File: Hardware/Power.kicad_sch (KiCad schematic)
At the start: 24 parts, among them IC1 TLV70130DBVR, IC2 TLV70130DBVR

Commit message: organization, updated submodule
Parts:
- D9: value 3V3 High -> 3V3 HV
- TP6: renamed from TP5; value 3V3 High -> 3V3 HV
- TP9: renamed from TP8; value GND High -> GND HV
- renumbered IC1 to IC2, IC2 to IC3, TP9 to TP10, TP4 to TP5, TP6 to TP7, TP7 to TP8
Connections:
- net +3V3 High renamed +3.3V HV
- net +3.3V HV: no longer TP6.1
- net +5V High renamed +5V HV
- net GND High renamed GND HV
- new net +3V3 HV: TP6.1
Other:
- note added: "3.3V: HV side"
- note added: "3.3V: LV side"
- note added: "HV 3V3"
- note added: "Indicators"
- note added: "Isolated"
- note added: "LV 3V3"
- note added: "MCU, CAN"
- note removed: "3.3V:"
- note removed: "Isolated 3v3"
- note removed: "Non-Isolated 3v3"
- note removed: "Status LEDs"

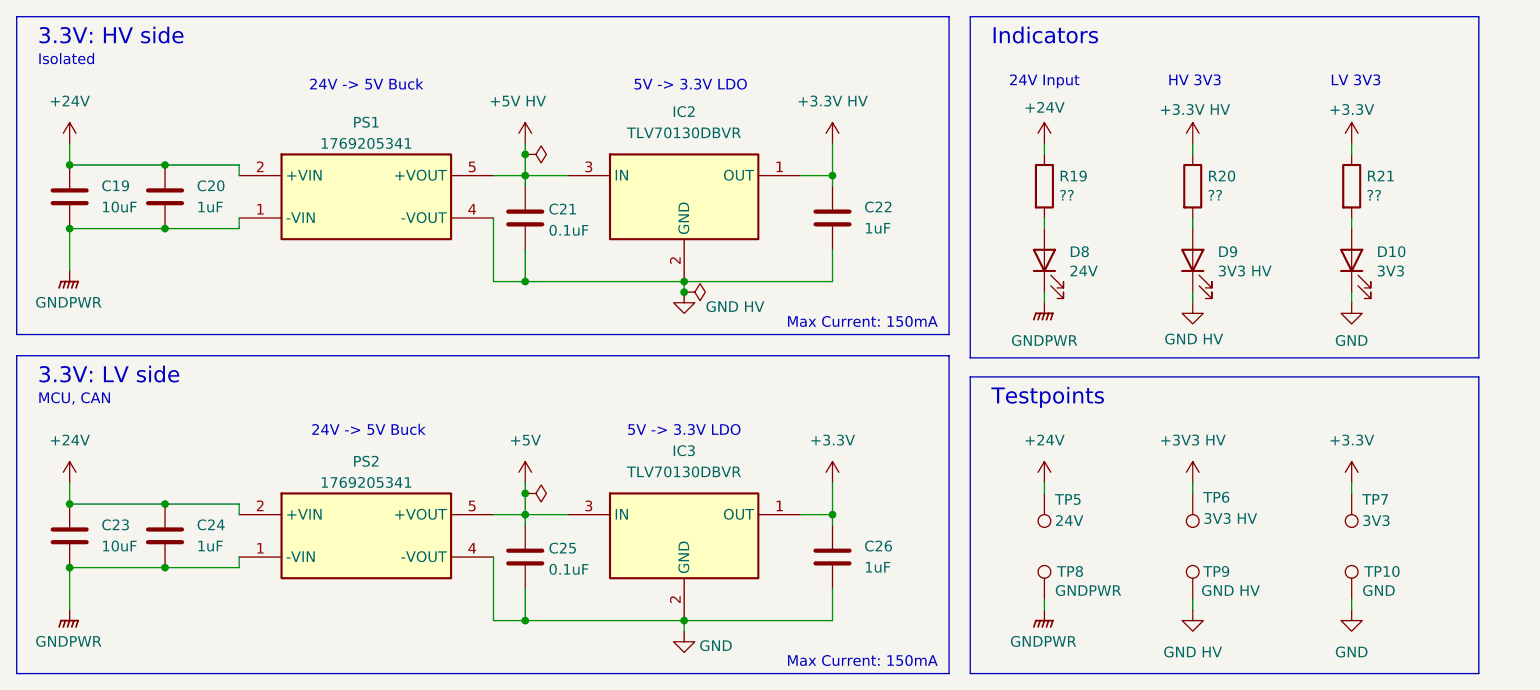
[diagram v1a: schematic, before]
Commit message: new isolated amp, filter stage; need to select values
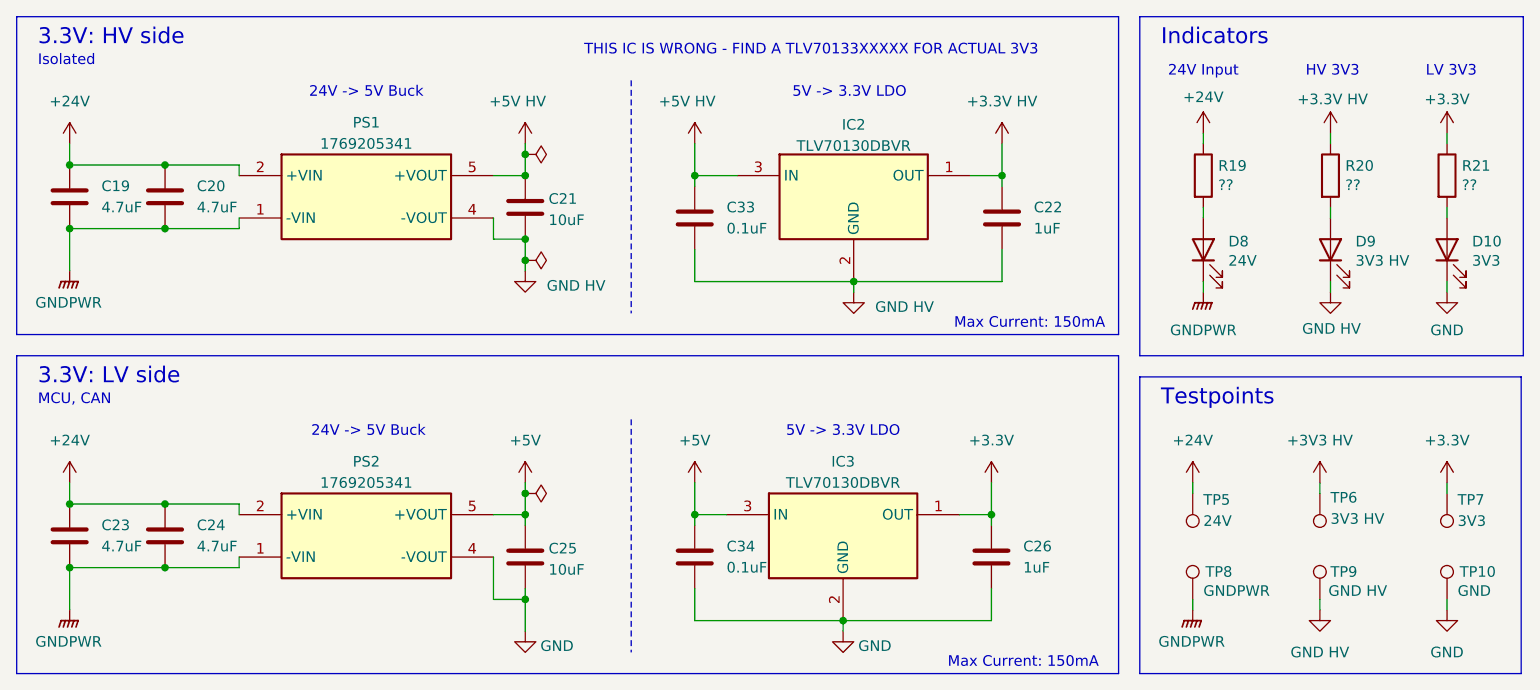
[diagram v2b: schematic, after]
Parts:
- added C33, C34: 0.1uF, Capacitor_SMD:C_0805_2012Metric, symbol Device:C
- C19, C23: value 10uF -> 4.7uF
- C20, C24: value 1uF -> 4.7uF
- C21, C25: value 0.1uF -> 10uF
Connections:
- net +5V: now also C34.1
- net +5V HV: now also C33.1
- net GND: now also C34.2
- net GND HV: now also C33.2
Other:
- note added: "THIS IC IS WRONG - FIND A TLV70133XXXXX FOR ACTUAL 3V3"
- moved on the sheet: C21, C22, C26, D10, D8, D9, IC2, IC3, R19, R20, R21, TP10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

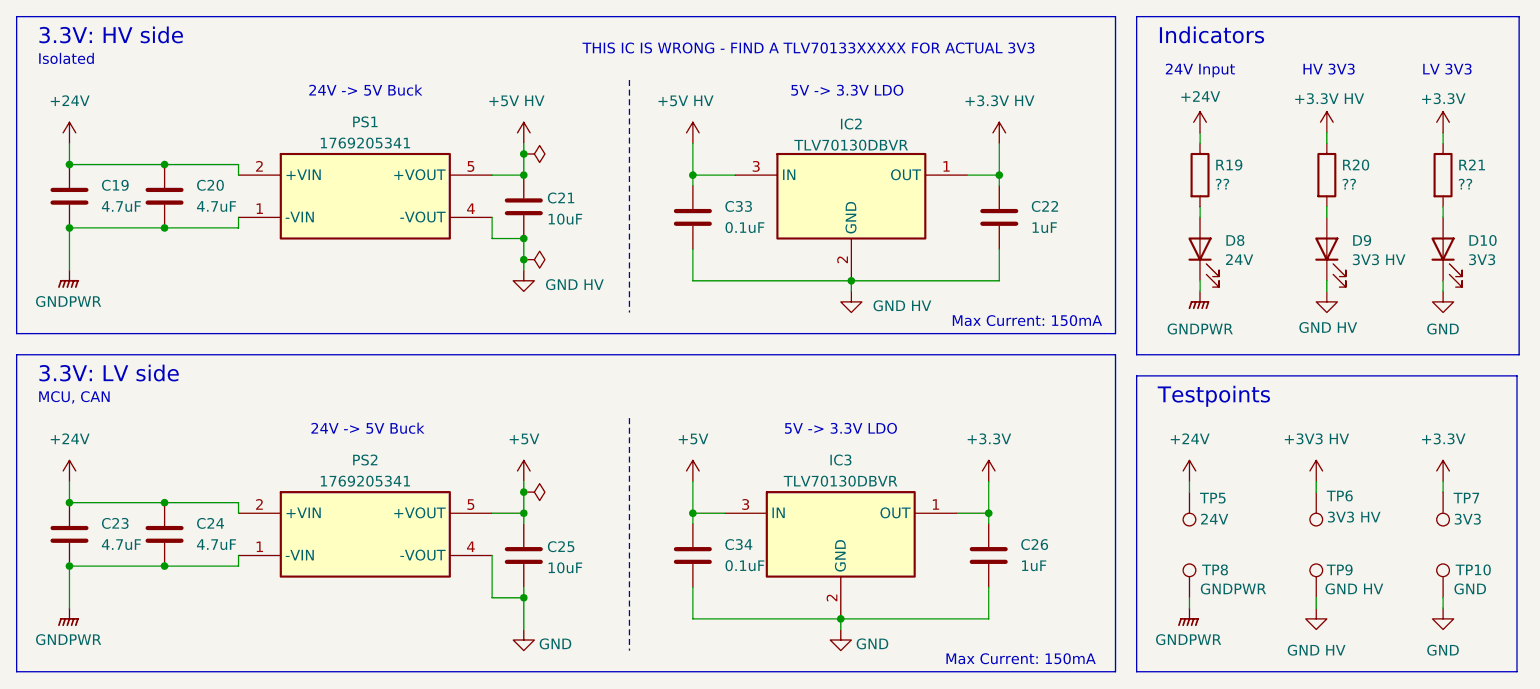
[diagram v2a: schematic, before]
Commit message: added LEDs, changed LDO, still need to address other comments
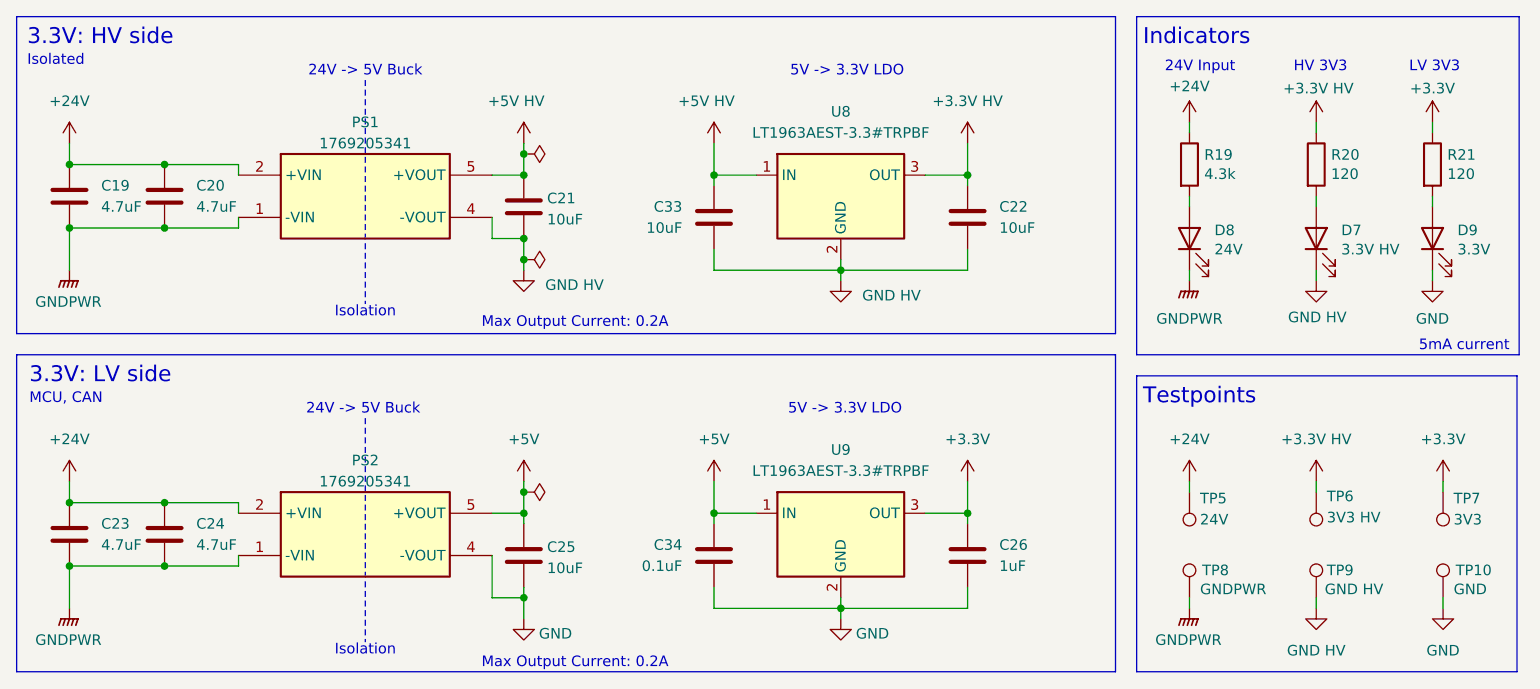
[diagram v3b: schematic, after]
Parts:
- removed D10: 3V3, LED_SMD:LED_0805_2012Metric, symbol Device:LED
- removed IC2, IC3: TLV70130DBVR, UTSVT_Power:TLV70130DBVR, symbol utsvt-power:TLV70130DBVR
- added D7: 3.3V HV, symbol Device:LED
- added U8, U9: LT1963AEST-3.3#TRPBF, Package_TO_SOT_SMD:SOT-223-3_TabPin2, symbol Regulator_Linear:LT1963AxST-3.3
- C22: value 1uF -> 10uF
- C33: value 0.1uF -> 10uF
- D8: footprint LED_SMD:LED_0805_2012Metric -> (none); Mfg APTD2012LCGCK -> XL-1608UBC-06A
- D9: value 3V3 HV -> 3.3V; footprint LED_SMD:LED_0805_2012Metric -> (none); Mfg APTD2012LCGCK -> XL-1608UBC-06A
- R19: value ?? -> 4.3k
- R20, R21: value ?? -> 120
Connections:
- net +3V3 HV is gone; now on net +3.3V HV: TP6.1
- net +3.3V: now also U9.3 (OUT)
- net +3.3V HV: now also U8.3 (OUT)
- net +5V: now also U9.1 (IN)
- net +5V HV: now also U8.1 (IN)
- net GND: now also D9.1 (K), U9.2 (GND)
- net GND HV: now also D7.1 (K), U8.2 (GND); no longer D9.1 (K)
- net at R21.2: now also D9.2 (A)
- net at R20.2: now also D7.2 (A); no longer D9.2 (A)
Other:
- note added: "5mA current"
- note added: "Isolation"
- note added: "Max Output Current: 0.2A"
- note removed: "Max Current: 150mA"
- note removed: "THIS IC IS WRONG - FIND A TLV70133XXXXX FOR ACTUAL 3V3"
- moved on the sheet: C22, C26, C33, C34, D8, R19, R20, R21

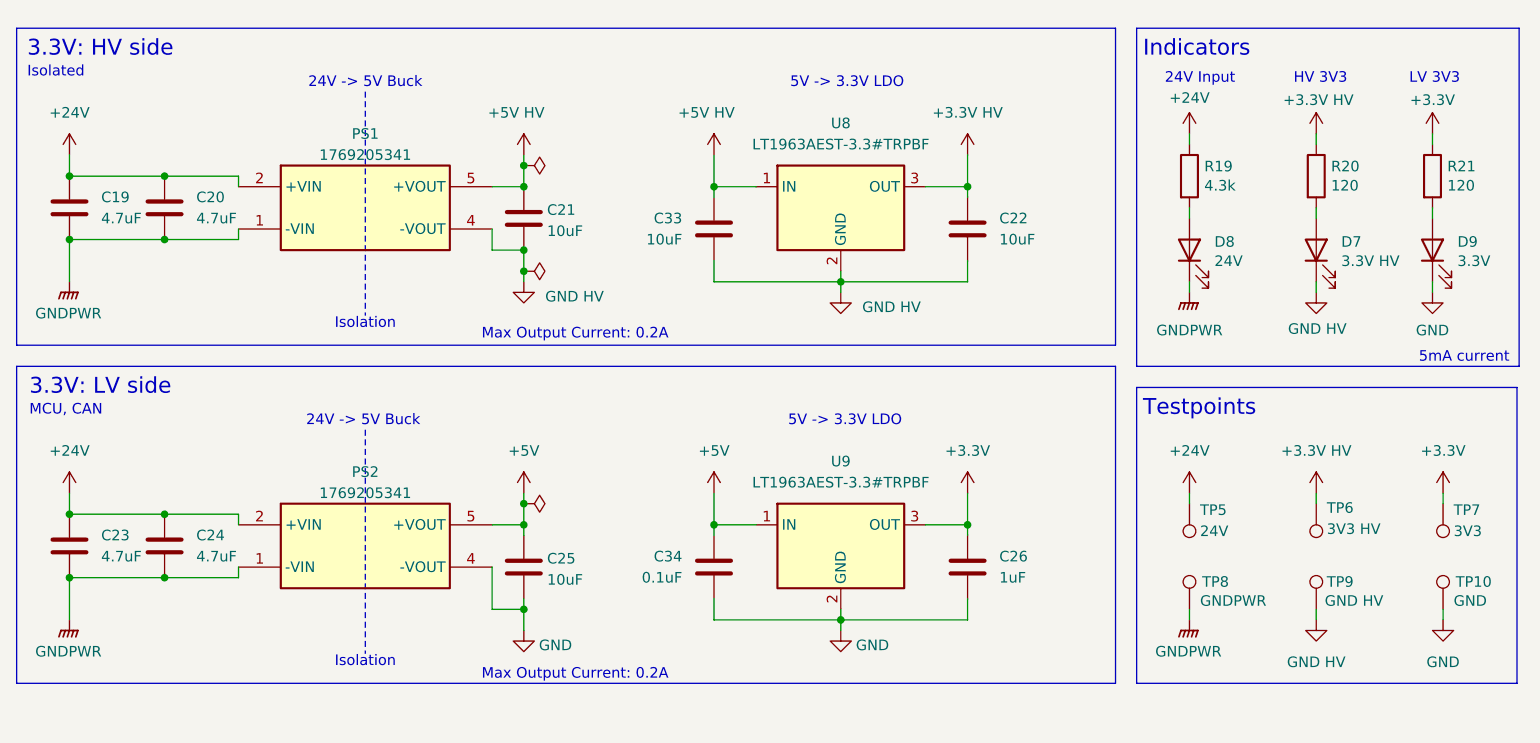
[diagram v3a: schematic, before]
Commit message: copied USB-C from psom
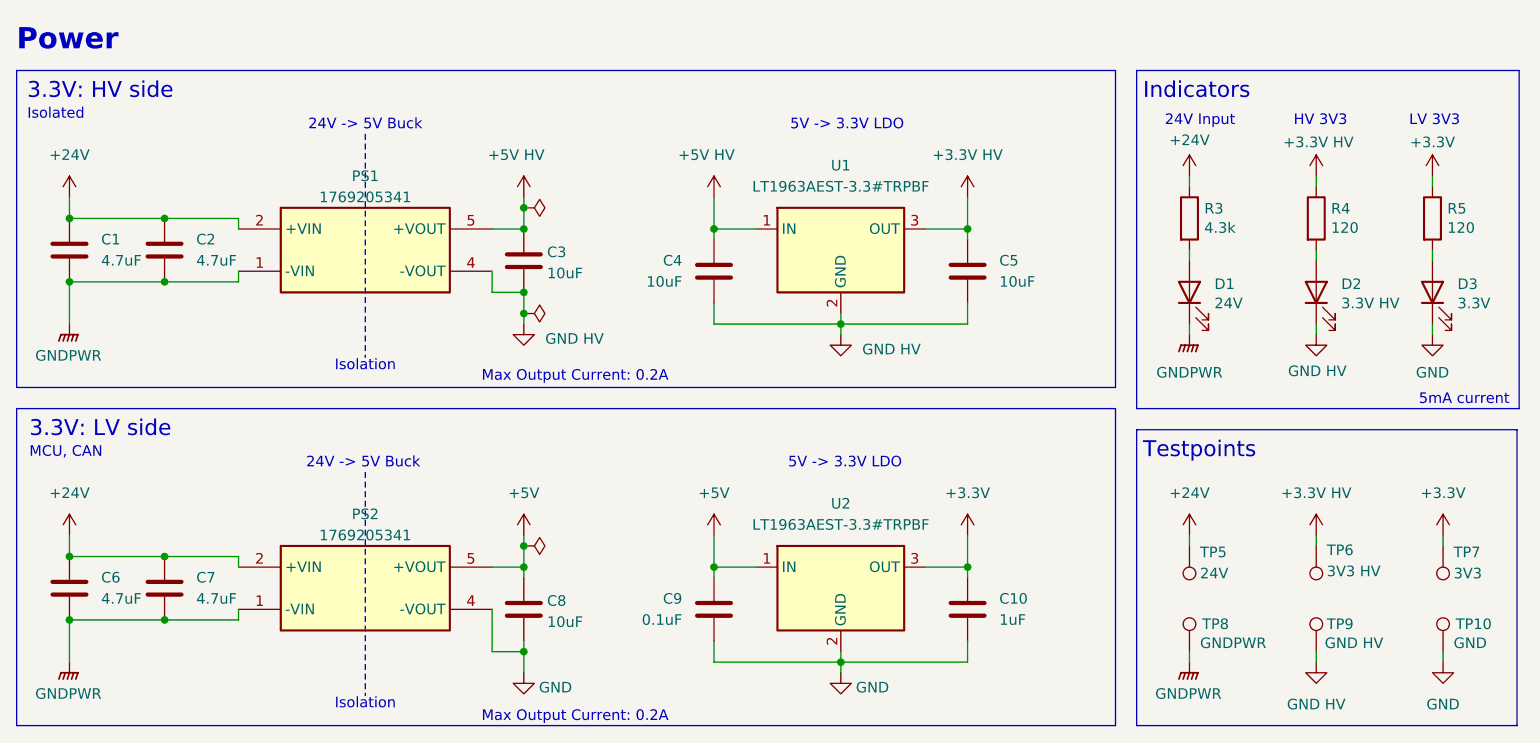
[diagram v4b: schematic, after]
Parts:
- renumbered C19 to C1, C26 to C10, C20 to C2, C21 to C3, C33 to C4, C22 to C5, C23 to C6, C24 to C7, C25 to C8, C34 to C9, D8 to D1, D7 to D2, D9 to D3, R19 to R3, R20 to R4, R21 to R5, U8 to U1, U9 to U2
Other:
- note added: "Power"
- moved on the sheet: C1, C10, C2, C3, C4, C5, C6, C7, C8, C9, D1, D2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

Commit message: something changed idk what though
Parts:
- removed PS1, PS2: 1769205341, 1769205341, symbol WE_24_5_Buck:1769205341
- added PS1, PS2: 1769205341, 1769205341, symbol WE_1769205341:1769205341
- renumbered C3 to C10, C4 to C11, C5 to C12, C6 to C13, C7 to C14, C8 to C15, C9 to C16, C10 to C17, C1 to C8, C2 to C9, D1 to D3, D2 to D4, D3 to D5, R5 to R10, R3 to R8, R4 to R9, TP8 to TP10, TP9 to TP11, TP10 to TP12, TP5 to TP7, TP6 to TP8, TP7 to TP9, U1 to U2, U2 to U3
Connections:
- net +24V: now also PS1.2 (+VIN), PS2.2 (+VIN)
- net +5V: now also PS2.5 (+VOUT)
- net +5V HV: now also PS1.5 (+VOUT)
- net GND: now also PS2.4 (-VOUT)
- net GND HV: now also PS1.4 (-VOUT)
- net GNDPWR: now also PS1.1 (-VIN), PS2.1 (-VIN)

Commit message: 0603 footprints
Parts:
- C10, C11, C12, C15, C16, C17: footprint Capacitor_SMD:C_0805_2012Metric -> Capacitor_SMD:C_0603_1608Metric_Pad1.08x0.95mm_HandSolder
- C13, C14, C8, C9: footprint (none) -> Capacitor_SMD:C_0603_1608Metric_Pad1.08x0.95mm_HandSolder
- D3, D4, D5: footprint (none) -> LED_SMD:LED_0603_1608Metric_Pad1.05x0.95mm_HandSolder
- PS1, PS2: footprint 1769205341 -> Parts:WE_1769205341
- R10, R8, R9: footprint Resistor_SMD:R_0805_2012Metric -> Resistor_SMD:R_0603_1608Metric_Pad0.98x0.95mm_HandSolder
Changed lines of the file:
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@@
 			)
 		)
-		(property "Footprint" ""
+		(property "Footprint" "Capacitor_SMD:C_0603_1608Metric_Pad1.08x0.95mm_HandSolder"
 			(at 33.9852 45.72 0)
 			(effects
@@
 			)
 		)
-		(property "Footprint" "Resistor_SMD:R_0805_2012Metric"
+		(property "Footprint" "Resistor_SMD:R_0603_1608Metric_Pad0.98x0.95mm_HandSolder"
 			(at 154.432 38.1 90)
 			(effects
@@
 			)
 		)
-		(property "Footprint" ""
+		(property "Footprint" "Capacitor_SMD:C_0603_1608Metric_Pad1.08x0.95mm_HandSolder"
 			(at 22.5552 86.36 0)
 			(effects
@@
 			)
 		)
-		(property "Footprint" ""
+		(property "Footprint" "Capacitor_SMD:C_0603_1608Metric_Pad1.08x0.95mm_HandSolder"
 			(at 33.9852 86.36 0)
 			(effects
@@
 			)
 		)
-		(property "Footprint" "Capacitor_SMD:C_0805_2012Metric"
+		(property "Footprint" "Capacitor_SMD:C_0603_1608Metric_Pad1.08x0.95mm_HandSolder"
 			(at 130.5052 48.26 0)
 			(effects
@@
 			)
 		)
-		(property "Footprint" ""
+		(property "Footprint" "LED_SMD:LED_0603_1608Metric_Pad1.05x0.95mm_HandSolder"
 			(at 185.42 46.99 0)
 			(effects
@@
 			)
 		)
-		(property "Footprint" ""
+		(property "Footprint" "LED_SMD:LED_0603_1608Metric_Pad1.05x0.95mm_HandSolder"
 			(at 171.45 46.99 0)
 			(effects
@@
 			)
 		)
-		(property "Footprint" "Capacitor_SMD:C_0805_2012Metric"
+		(property "Footprint" "Capacitor_SMD:C_0603_1608Metric_Pad1.08x0.95mm_HandSolder"
 			(at 98.0948 88.9 0)
 			(effects
@@
 			)
 		)
-		(property "Footprint" "Capacitor_SMD:C_0805_2012Metric"
+		(property "Footprint" "Capacitor_SMD:C_0603_1608Metric_Pad1.08x0.95mm_HandSolder"
 			(at 98.0948 48.26 0)
 			(effects
@@
 			)
 		)
-		(property "Footprint" ""
+		(property "Footprint" "LED_SMD:LED_0603_1608Metric_Pad1.05x0.95mm_HandSolder"
 			(at 156.21 46.99 0)
 			(effects
@@
 			)
 		)
-		(property "Footprint" "Capacitor_SMD:C_0805_2012Metric"
+		(property "Footprint" "Capacitor_SMD:C_0603_1608Metric_Pad1.08x0.95mm_HandSolder"
 			(at 75.2348 88.9 0)
 			(effects
@@
 			)
 		)
-		(property "Footprint" ""
+		(property "Footprint" "Capacitor_SMD:C_0603_1608Metric_Pad1.08x0.95mm_HandSolder"
 			(at 22.5552 45.72 0)
 			(effects
@@
 			)
 		)
-		(property "Footprint" "Capacitor_SMD:C_0805_2012Metric"
+		(property "Footprint" "Capacitor_SMD:C_0603_1608Metric_Pad1.08x0.95mm_HandSolder"
 			(at 75.2348 46.99 0)
 			(effects
@@
 			)
 		)
-		(property "Footprint" "Resistor_SMD:R_0805_2012Metric"
+		(property "Footprint" "Resistor_SMD:R_0603_1608Metric_Pad0.98x0.95mm_HandSolder"
 			(at 169.672 38.1 90)
 			(effects
@@
 			)
 		)
-		(property "Footprint" "Capacitor_SMD:C_0805_2012Metric"
+		(property "Footprint" "Capacitor_SMD:C_0603_1608Metric_Pad1.08x0.95mm_HandSolder"
 			(at 130.5052 88.9 0)
 			(effects
@@
 			)
 		)
-		(property "Footprint" "Resistor_SMD:R_0805_2012Metric"
+		(property "Footprint" "Resistor_SMD:R_0603_1608Metric_Pad0.98x0.95mm_HandSolder"
 			(at 183.642 38.1 90)
 			(effects
@@
 			)
 		)
-		(property "Footprint" "1769205341"
+		(property "Footprint" "Parts:WE_1769205341"
 			(at 68.58 134.29 0)
 			(effects
@@
 			)
 		)
-		(property "Footprint" "1769205341"
+		(property "Footprint" "Parts:WE_1769205341"
 			(at 68.58 174.93 0)
 			(effects
